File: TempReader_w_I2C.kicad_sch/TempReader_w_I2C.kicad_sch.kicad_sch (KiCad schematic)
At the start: 49 parts, among them J1 NRF Pin Header, J2 BME Pin Header, J3 PowerHeader, SW1 D6R90F2LFS, U5 MIC5205-3.3YM5, Y2 16Mhz

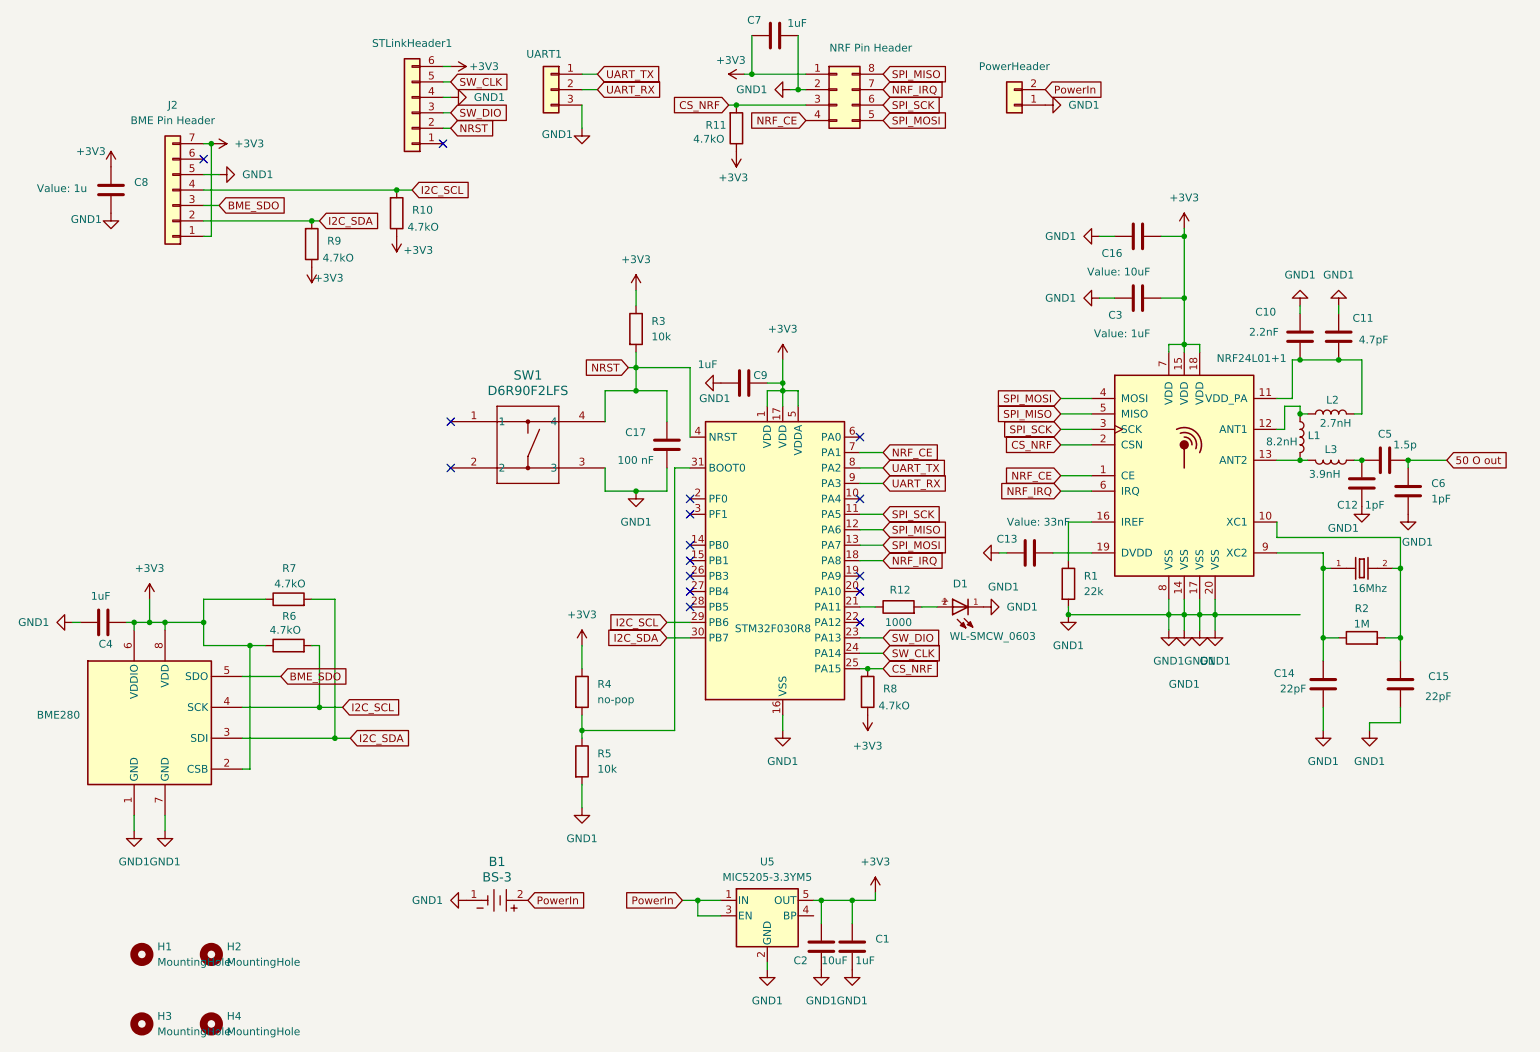
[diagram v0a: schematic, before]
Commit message: Change data rate and signal strength
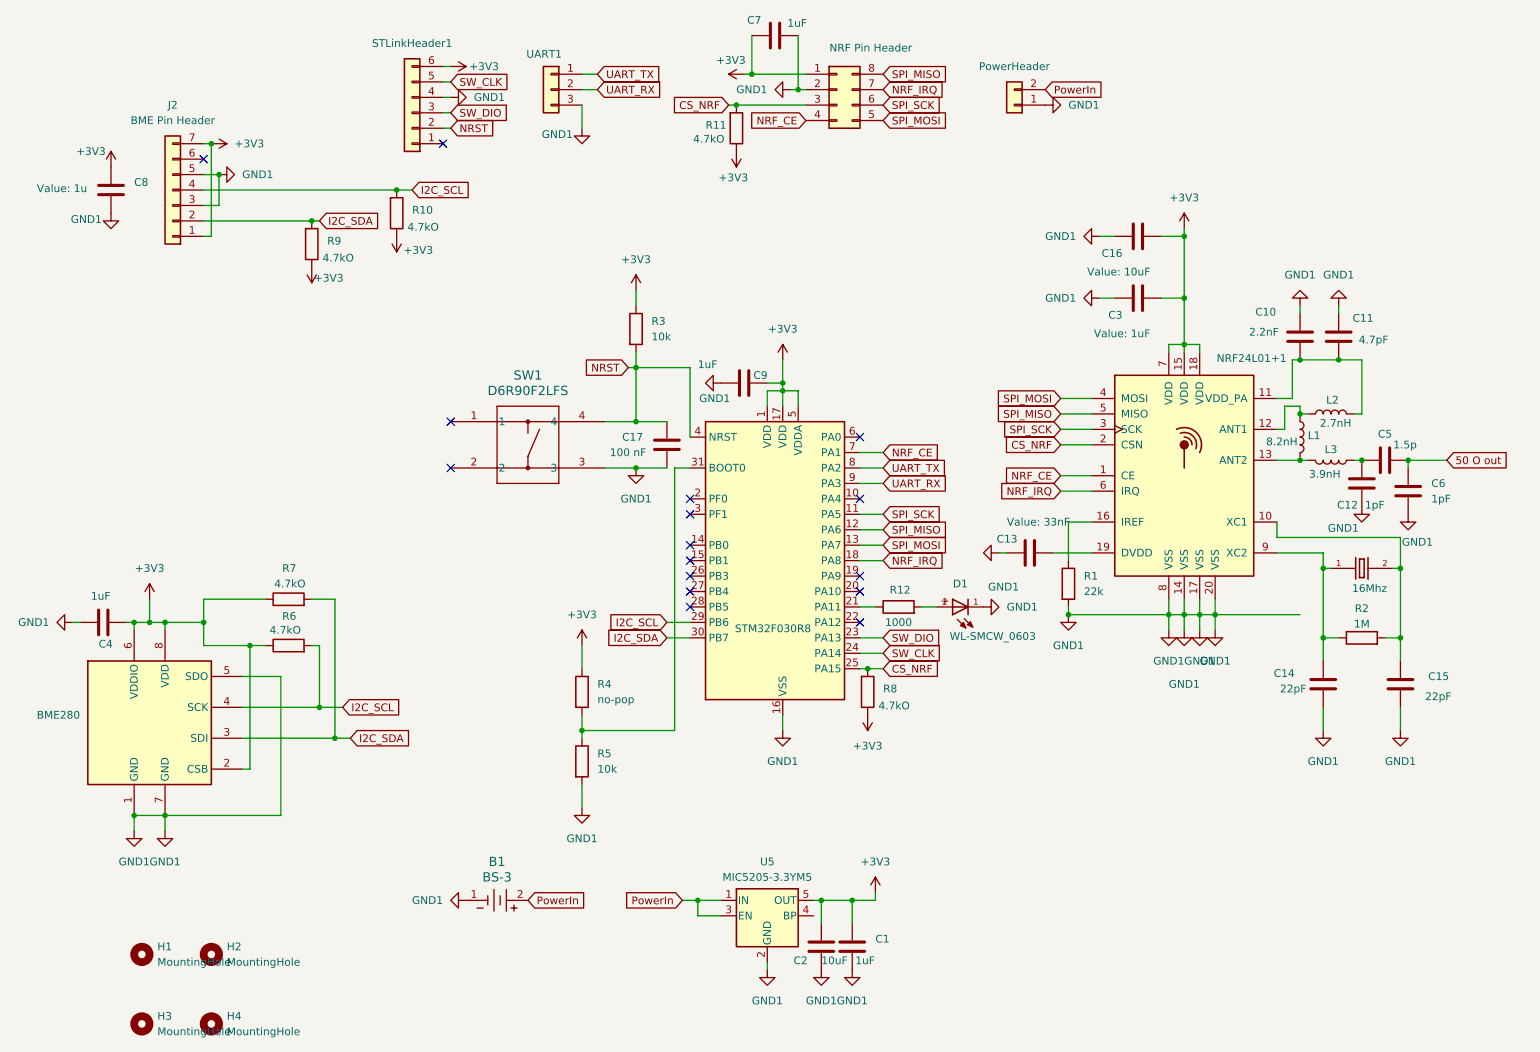
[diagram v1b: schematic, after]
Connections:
- net BME_SDO is gone; now on net GND1: BME280.5 (SDO), J2.3 (Pin_3)
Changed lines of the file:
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@@
 	)
 	(junction
+		(at 45.72 40.64)
+		(diameter 0)
+		(color 0 0 0 0)
+	)
+	(junction
 		(at 144.78 160.02)
 		(diameter 0)
@@
 	)
 	(junction
+		(at 114.3 81.28)
+		(diameter 0)
+		(color 0 0 0 0)
+	)
+	(junction
 		(at 133.35 24.13)
 		(diameter 0)
@@
 	)
 	(junction
-		(at 114.3 92.71)
+		(at 36.83 146.05)
 		(diameter 0)
 		(color 0 0 0 0)
 	)
 	(junction
-		(at 114.3 76.2)
+		(at 31.75 146.05)
 		(diameter 0)
 		(color 0 0 0 0)
@@
 	)
 	(junction
+		(at 114.3 88.9)
+		(diameter 0)
+		(color 0 0 0 0)
+	)
+	(junction
 		(at 114.3 72.39)
 		(diameter 0)
@@
 	(wire
 		(pts
+			(xy 55.88 146.05) (xy 36.83 146.05)
+		)
+		(stroke
+			(width 0)
+			(type default)
+		)
+	)
+	(wire
+		(pts
 			(xy 64.77 133.35) (xy 67.31 133.35)
 		)
@@
 	(wire
 		(pts
+			(xy 31.75 146.05) (xy 36.83 146.05)
+		)
+		(stroke
+			(width 0)
+			(type default)
+		)
+	)
+	(wire
+		(pts
 			(xy 43.18 43.18) (xy 74.93 43.18)
 		)
@@
 	(wire
 		(pts
-			(xy 114.3 92.71) (xy 119.38 92.71)
+			(xy 114.3 88.9) (xy 119.38 88.9)
 		)
 		(stroke
@@
 	(wire
 		(pts
-			(xy 119.38 81.28) (xy 119.38 76.2)
-		)
-		(stroke
-			(width 0)
-			(type default)
-		)
-	)
-	(wire
-		(pts
 			(xy 200.66 50.8) (xy 204.47 50.8)
 		)
@@
 	(wire
 		(pts
-			(xy 234.95 130.81) (xy 234.95 132.08)
+			(xy 240.03 128.27) (xy 240.03 132.08)
 		)
 		(stroke
@@
 	(wire
 		(pts
-			(xy 31.75 114.3) (xy 31.75 115.57)
+			(xy 45.72 40.64) (xy 45.72 45.72)
 		)
 		(stroke
@@
 	(wire
 		(pts
-			(xy 151.13 104.14) (xy 154.94 104.14)
+			(xy 31.75 114.3) (xy 31.75 115.57)
 		)
 		(stroke
@@
 	(wire
 		(pts
-			(xy 123.19 72.39) (xy 123.19 83.82)
+			(xy 151.13 104.14) (xy 154.94 104.14)
 		)
 		(stroke
@@
 	(wire
 		(pts
-			(xy 233.68 80.01) (xy 232.41 80.01)
+			(xy 123.19 72.39) (xy 123.19 83.82)
 		)
 		(stroke
@@
 	(wire
 		(pts
-			(xy 105.41 29.21) (xy 105.41 33.02)
+			(xy 233.68 80.01) (xy 232.41 80.01)
 		)
 		(stroke
@@
 	(wire
 		(pts
-			(xy 135.89 170.18) (xy 135.89 171.45)
+			(xy 105.41 29.21) (xy 105.41 33.02)
 		)
 		(stroke
@@
 	(wire
 		(pts
-			(xy 60.96 110.49) (xy 64.77 110.49)
+			(xy 135.89 170.18) (xy 135.89 171.45)
 		)
 		(stroke
@@
 	(wire
 		(pts
-			(xy 124.46 160.02) (xy 128.27 160.02)
+			(xy 55.88 123.19) (xy 55.88 146.05)
 		)
 		(stroke
@@
 	(wire
 		(pts
-			(xy 49.53 133.35) (xy 64.77 133.35)
+			(xy 60.96 110.49) (xy 64.77 110.49)
 		)
 		(stroke
@@
 	(wire
 		(pts
-			(xy 45.72 45.72) (xy 43.18 45.72)
+			(xy 124.46 160.02) (xy 128.27 160.02)
 		)
 		(stroke
@@
 	(wire
 		(pts
-			(xy 43.18 110.49) (xy 43.18 114.3)
+			(xy 49.53 133.35) (xy 64.77 133.35)
 		)
 		(stroke
@@
 	(wire
 		(pts
-			(xy 200.66 60.96) (xy 204.47 60.96)
+			(xy 45.72 45.72) (xy 43.18 45.72)
 		)
 		(stroke
@@
 	(wire
 		(pts
-			(xy 240.03 130.81) (xy 234.95 130.81)
+			(xy 43.18 110.49) (xy 43.18 114.3)
 		)
 		(stroke
@@
 	(wire
 		(pts
-			(xy 151.13 101.6) (xy 154.94 101.6)
+			(xy 200.66 60.96) (xy 204.47 60.96)
 		)
 		(stroke
@@
 	(wire
 		(pts
-			(xy 240.03 128.27) (xy 240.03 130.81)
+			(xy 151.13 101.6) (xy 154.94 101.6)
 		)
 		(stroke
@@
 	(wire
 		(pts
-			(xy 119.38 76.2) (xy 114.3 76.2)
+			(xy 119.38 81.28) (xy 114.3 81.28)
 		)
 		(stroke
@@
 	(wire
 		(pts
-			(xy 119.38 88.9) (xy 119.38 92.71)
-		)
-		(stroke
-			(width 0)
-			(type default)
-		)
-	)
-	(wire
-		(pts
 			(xy 36.83 146.05) (xy 36.83 148.59)
 		)
@@
 	(wire
 		(pts
-			(xy 114.3 76.2) (xy 114.3 72.39)
-		)
-		(stroke
-			(width 0)
-			(type default)
-		)
-	)
-	(wire
-		(pts
 			(xy 184.15 92.71) (xy 189.23 92.71)
 		)
@@
 	(wire
 		(pts
+			(xy 114.3 72.39) (xy 114.3 81.28)
+		)
+		(stroke
+			(width 0)
+			(type default)
+		)
+	)
+	(wire
+		(pts
 			(xy 209.55 110.49) (xy 209.55 113.03)
 		)
@@
 	(wire
 		(pts
-			(xy 109.22 76.2) (xy 114.3 76.2)
+			(xy 109.22 81.28) (xy 114.3 81.28)
 		)
 		(stroke
@@
 	(wire
 		(pts
-			(xy 109.22 92.71) (xy 114.3 92.71)
-		)
-		(stroke
-			(width 0)
-			(type default)
-		)
-	)
-	(wire
-		(pts
-			(xy 109.22 92.71) (xy 109.22 88.9)
+			(xy 109.22 88.9) (xy 114.3 88.9)
 		)
 		(stroke
@@
 	(wire
 		(pts
-			(xy 109.22 81.28) (xy 109.22 76.2)
-		)
-		(stroke
-			(width 0)
-			(type default)
-		)
-	)
-	(wire
-		(pts
 			(xy 190.5 60.96) (xy 193.04 60.96)
 		)
@@
 		)
 	)
-	(global_label "BME_SDO"
-		(shape input)
-		(at 45.72 45.72 0)
-		(fields_autoplaced yes)
-		(effects
-			(font
-				(size 1.27 1.27)
-			)
-			(justify left)
-		)
-		(property "Intersheetrefs" "${INTERSHEET_REFS}"
-			(at 57.3532 45.72 0)
-			(effects
-				(font
-					(size 1.27 1.27)
-				)
-				(justify left)
-				(hide yes)
-			)
-		)
-	)
 	(global_label "SPI_MISO"
 		(shape input)
@@
 		)
 	)
-	(global_label "BME_SDO"
-		(shape input)
-		(at 55.88 123.19 0)
-		(fields_autoplaced yes)
-		(effects
-			(font
-				(size 1.27 1.27)
-			)
-			(justify left)
-		)
-		(property "Intersheetrefs" "${INTERSHEET_REFS}"
-			(at 67.5132 123.19 0)
-			(effects
-				(font
-					(size 1.27 1.27)
-				)
-				(justify left)
-				(hide yes)
-			)
-		)
-	)
 	(symbol
 		(lib_id "power:GND1")
@@
 	(symbol
 		(lib_id "power:GND1")
-		(at 234.95 132.08 0)
+		(at 240.03 132.08 0)
 		(unit 1)
 		(exclude_from_sim no)
@@
 		(fields_autoplaced yes)
 		(property "Reference" "#PWR027"
-			(at 234.95 138.43 0)
+			(at 240.03 138.43 0)
 			(effects
 				(font
@@
 		)
 		(property "Value" "GND1"
-			(at 234.95 137.16 0)
+			(at 240.03 137.16 0)
 			(effects
 				(font
@@
 		)
 		(property "Footprint" ""
-			(at 234.95 132.08 0)
+			(at 240.03 132.08 0)
 			(effects
 				(font
@@
 		)
 		(property "Datasheet" ""
-			(at 234.95 132.08 0)
+			(at 240.03 132.08 0)
 			(effects
 				(font
@@
 		)
 		(property "Description" "Power symbol creates a global label with name \"GND1\" , ground"
-			(at 234.95 132.08 0)
+			(at 240.03 132.08 0)
 			(effects
 				(font
@@
 		(dnp no)
 		(property "Reference" "C17"
-			(at 112.522 83.058 0)
+			(at 112.014 83.82 0)
 			(effects
 				(font
@@
 		)
 		(property "Value" "100 nF"
-			(at 111.252 87.63 0)
+			(at 109.982 86.36 0)
 			(effects
 				(font
@@
 	(symbol
 		(lib_id "power:GND1")
-		(at 114.3 92.71 0)
+		(at 114.3 88.9 0)
 		(unit 1)
 		(exclude_from_sim no)
@@
 		(fields_autoplaced yes)
 		(property "Reference" "#PWR045"
-			(at 114.3 99.06 0)
+			(at 114.3 95.25 0)
 			(effects
 				(font
@@
 		)
 		(property "Value" "GND1"
-			(at 114.3 97.79 0)
+			(at 114.3 93.98 0)
 			(effects
 				(font
@@
 		)
 		(property "Footprint" ""
-			(at 114.3 92.71 0)
+			(at 114.3 88.9 0)
 			(effects
 				(font
@@
 		)
 		(property "Datasheet" ""
-			(at 114.3 92.71 0)
+			(at 114.3 88.9 0)
 			(effects
 				(font
@@
 		)
 		(property "Description" "Power symbol creates a global label with name \"GND1\" , ground"
-			(at 114.3 92.71 0)
+			(at 114.3 88.9 0)
 			(effects
 				(font
